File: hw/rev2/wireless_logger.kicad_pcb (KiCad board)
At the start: 4 copper layers, 147 parts, among them J1 FCI 10118194, J2 CONN_2, J3 SSD1306_SER, J4 SWD_10PIN, J5 CONN_5, P1 CONN_6X2, Q1 2N7002P, Q2 2N7002P, U1 MT29FXX01A, U10 CC2541, U11 STM32F40X_BGA176, U2 MAG3110, U3 MMA8452Q, U4 LPS331AP, U5 L3GD20, U6 MCP111T-315, U7 BQ24095, U8 TPS62698, U9 CC1101, X1 FA-128 26.0000MF10Z-W3, X2 9HT10-32.768KBZF-T, X3 FA-128 32.0000MF20X-K3, X4 XRCGB25M000F0L00R0, X5 9HT10-32.768KBZF-T

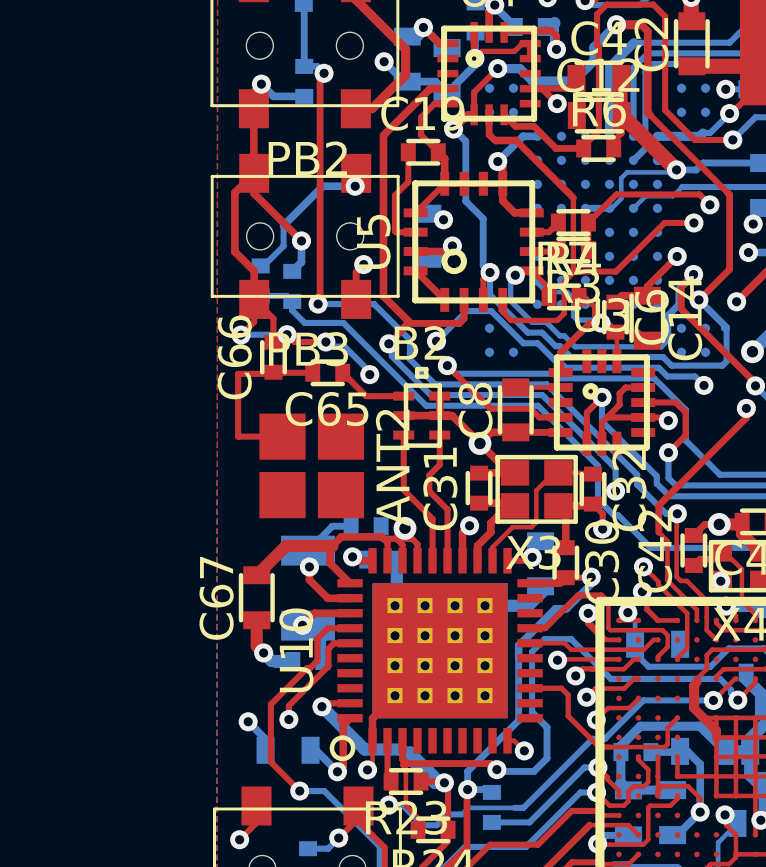
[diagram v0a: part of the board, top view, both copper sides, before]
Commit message: Minor rerouting stuffs
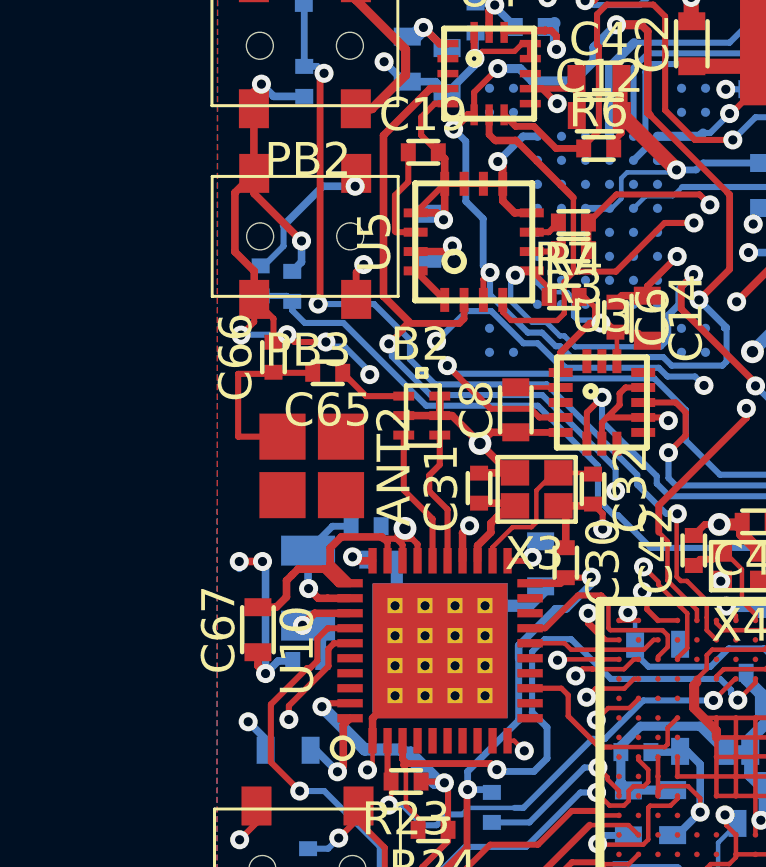
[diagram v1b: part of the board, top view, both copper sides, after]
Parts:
- moved C67 1.07 mm to (171.4, 138.8)
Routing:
- net GND: track 262.2 -> 268.0 mm, vias 54 -> 56
- net V3: track 321.9 -> 323.9 mm

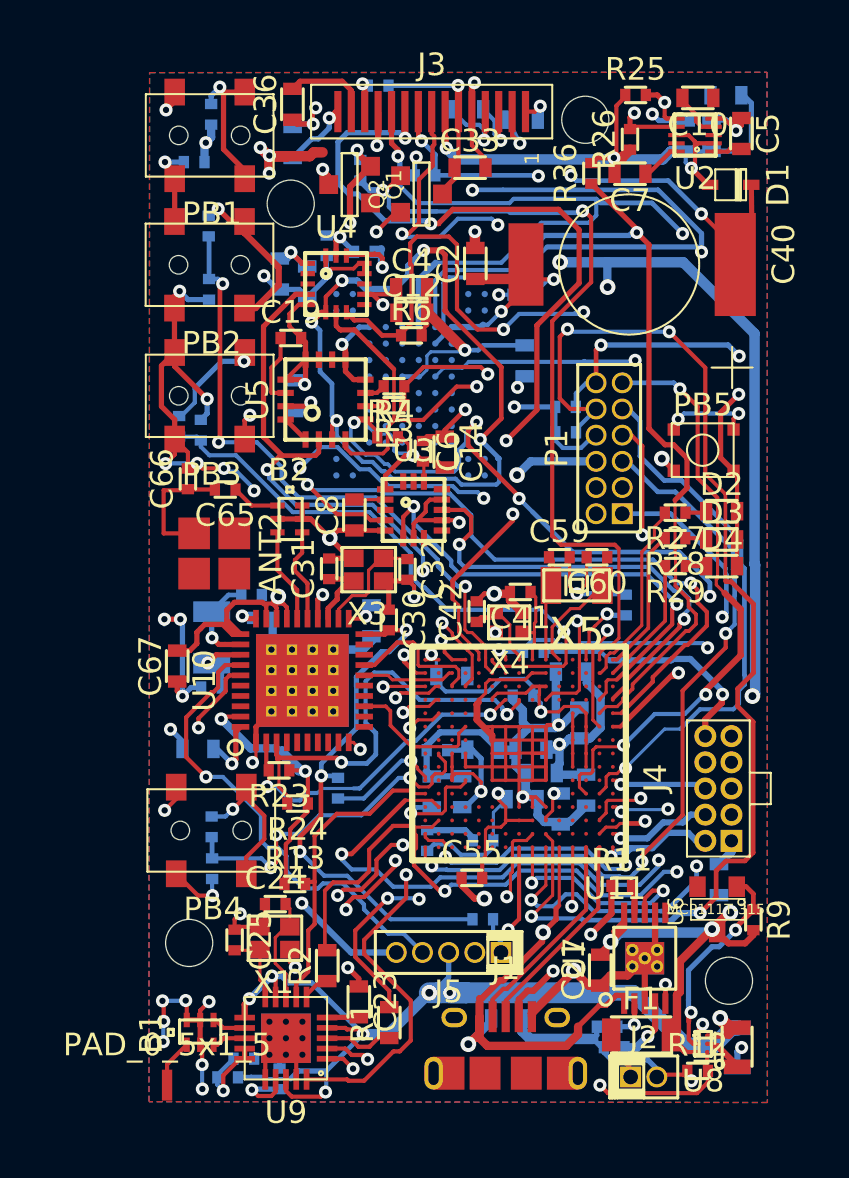
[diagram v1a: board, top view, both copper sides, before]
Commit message: STM32 checked -- Some optimization done on routes and important filtering bits
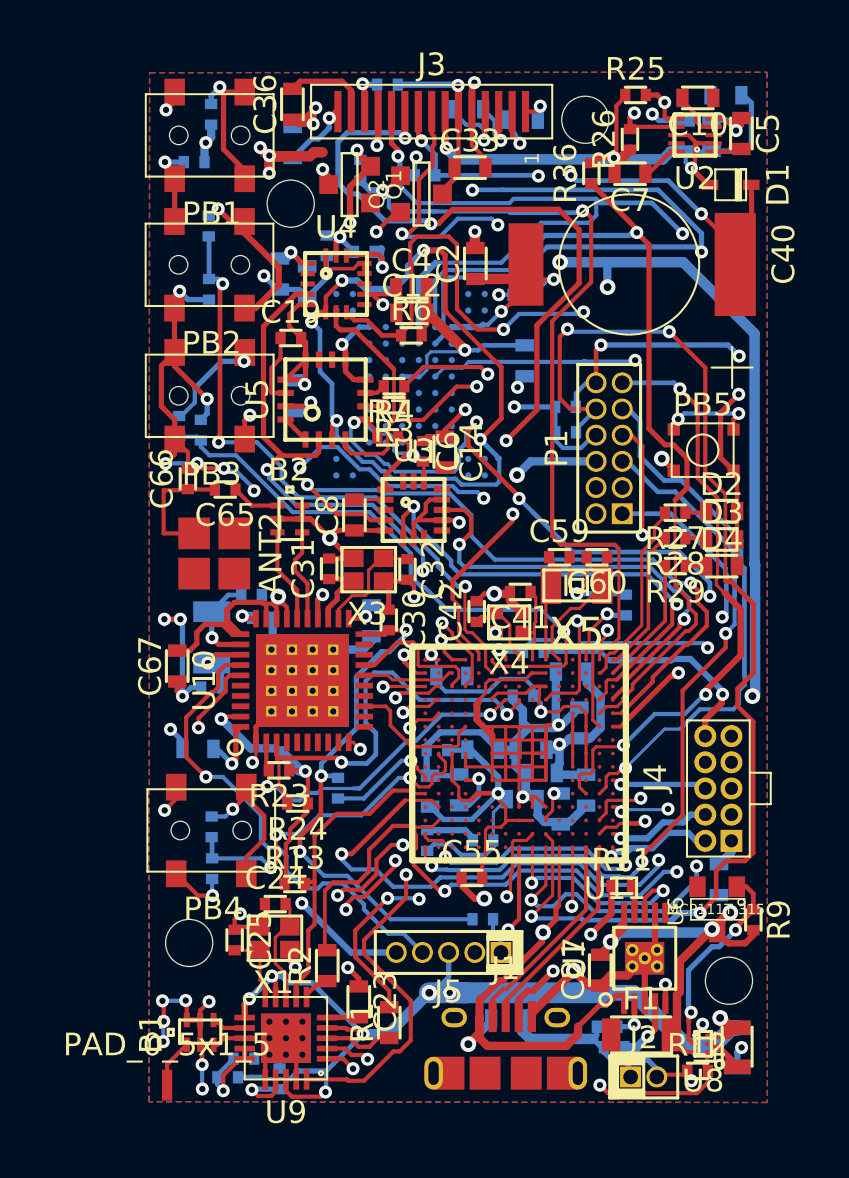
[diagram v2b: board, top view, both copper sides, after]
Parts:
- moved C45 1.55 mm to (183.6, 144.9)
- moved C44 1.33 mm to (185.1, 144.8)
- moved R21 0.45 mm to (181.6, 110.6)
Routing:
- net V3: track 323.9 -> 328.2 mm, vias 29 -> 28
- net N-0000063: track 5.17 -> 2.65 mm
- net /OLED/OLED_GND: track 17.4 -> 19.3 mm
- net GND: track 268.0 -> 269.3 mm

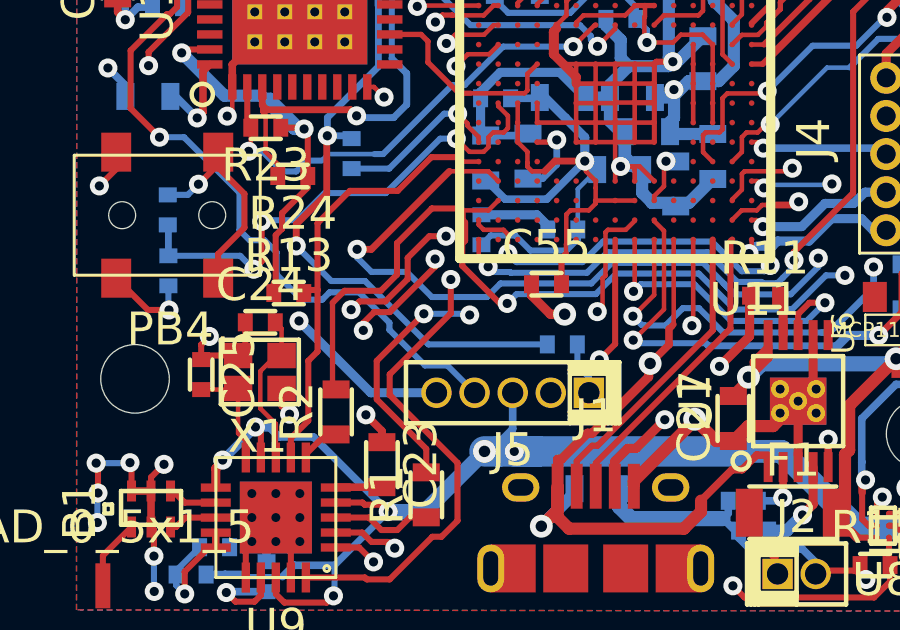
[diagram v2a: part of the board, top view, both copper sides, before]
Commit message: Fixed misconnected CC1101 debug output to SPI2
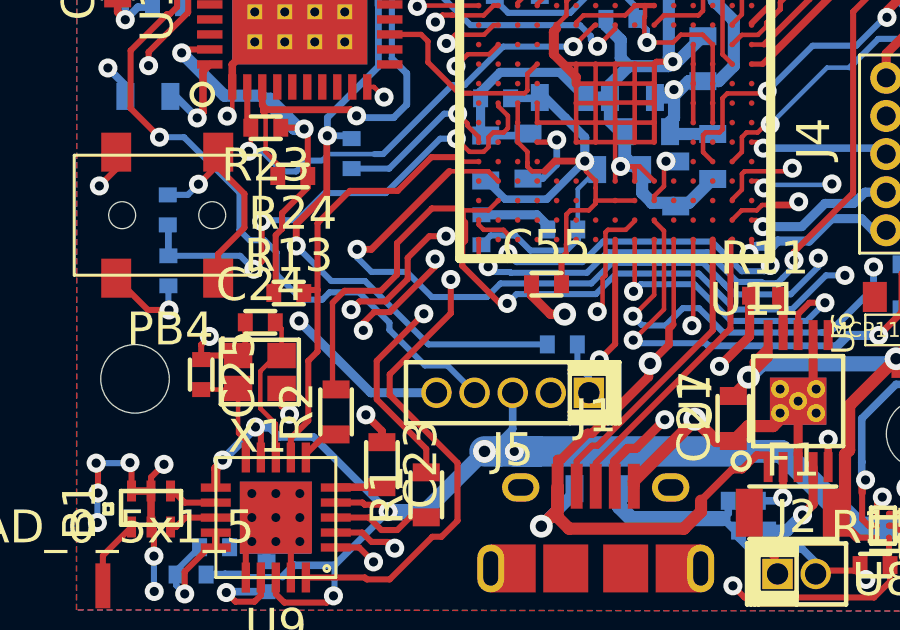
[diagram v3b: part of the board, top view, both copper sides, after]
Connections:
- R1 pad 2: /STM32F4/SPI2_MISO -> /STM32F4/SPI2_MOSI
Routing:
- net /STM32F4/SPI2_MISO: track 42.8 -> 32.1 mm, vias 4 -> 2
- net /STM32F4/SPI2_MOSI: track 36.6 -> 46.4 mm, vias 3 -> 4

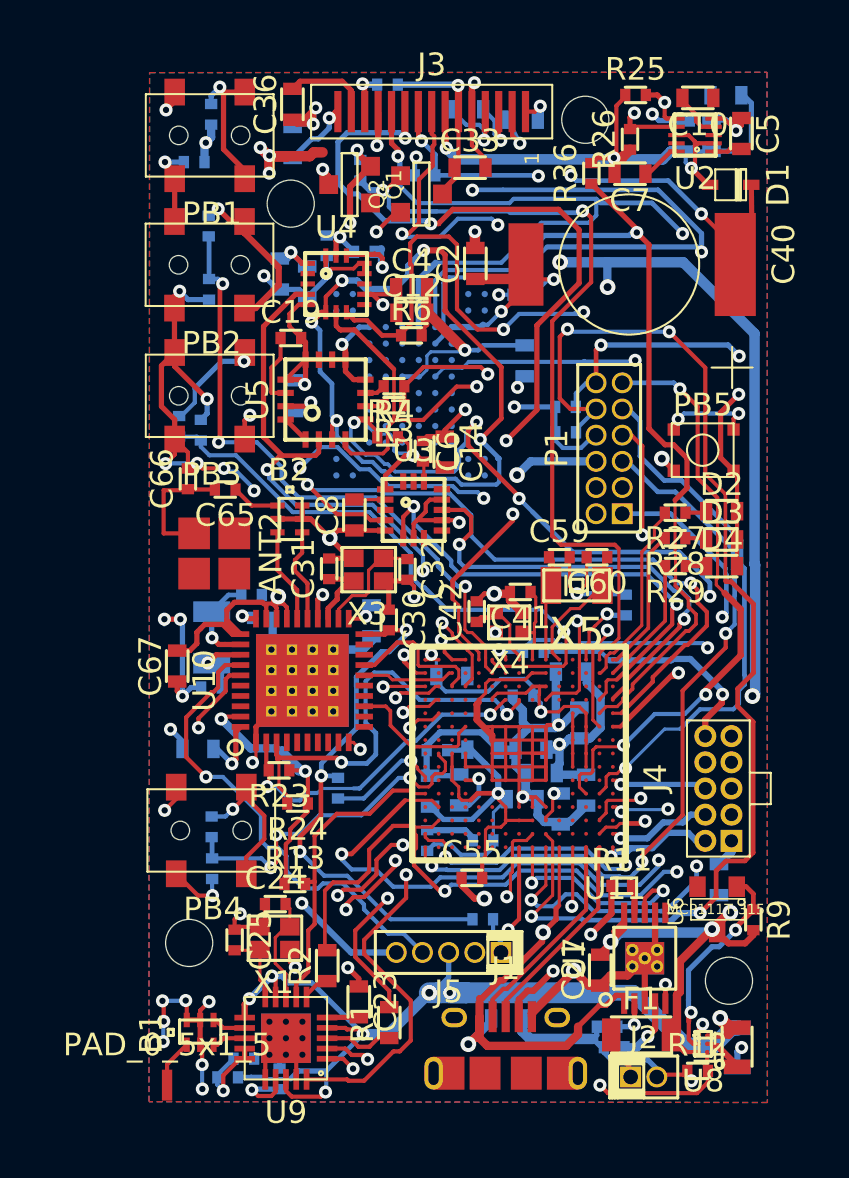
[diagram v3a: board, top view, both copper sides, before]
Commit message: Moved silks around!
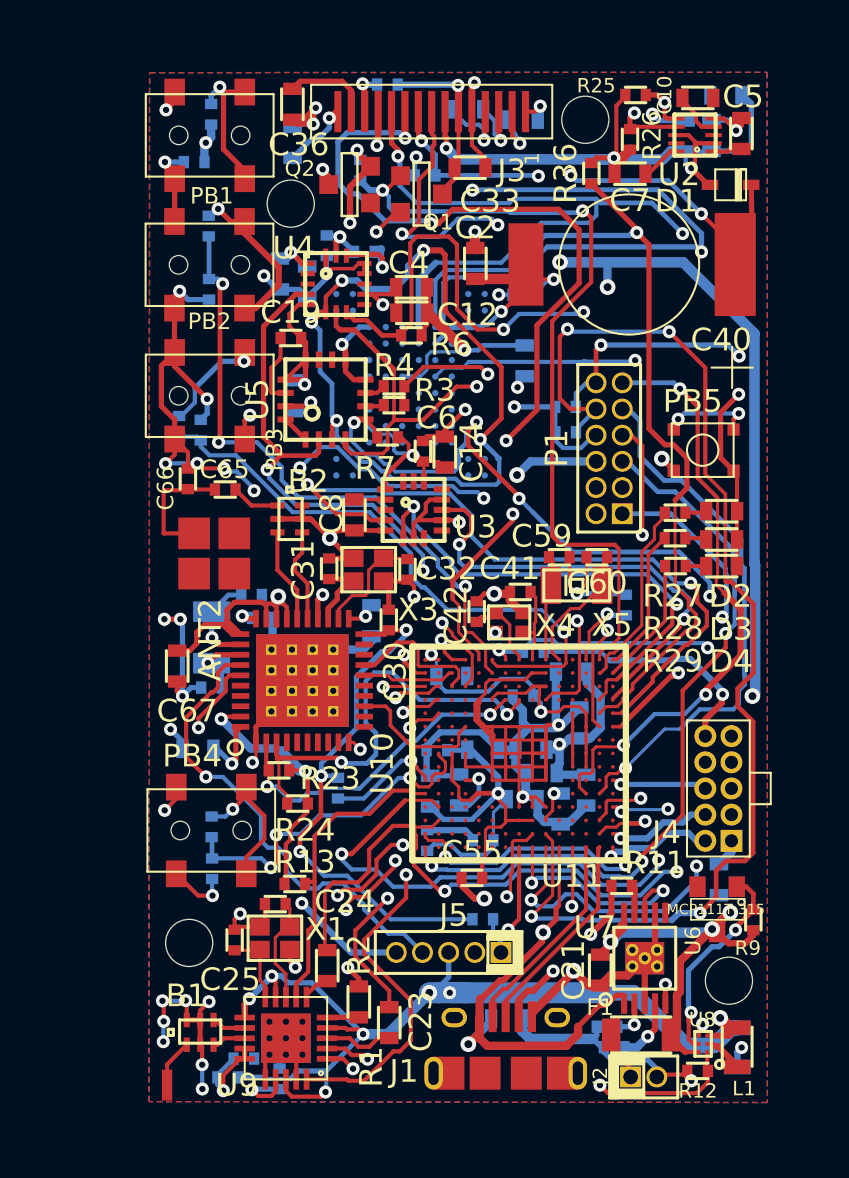
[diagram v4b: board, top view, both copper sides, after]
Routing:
- net (no net): track 5.00 -> 0.01 mm, vias 3 -> 0
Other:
- board text added: "+"
- board text added: "-"
- board text added: "2013 McGill IML"
- board text added: "rev 2a"

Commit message: Rev 2a submitted to OSH Park for manufacture
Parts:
- moved C50 0.92 mm to (188.0, 146.2)
- moved C6 0.16 mm to (183.3, 128.3)
- renumbered P1 to J6
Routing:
- net GND: track 269.3 -> 282.2 mm
- net N-00000167: track 28.6 -> 34.2 mm
- net /Sensors/GYR_SPI_MOSI: track 80.8 -> 85.1 mm, vias 7 -> 6
- net V3: track 328.2 -> 332.4 mm
- net /STM32F4/SPI2_NSS: track 51.5 -> 53.5 mm
- net /STM32F4/EXTI8: track 16.8 -> 18.6 mm
- net N-00000189: track 10.3 -> 12.1 mm
- net /STM32F4/OLED_nD/C: track 47.0 -> 48.6 mm
- net /Sensors/ACC_INT1: track 22.3 -> 23.8 mm
- net /Sensors/ACC_I2C_SCL: track 66.3 -> 67.7 mm
- net /Sensors/GYR_SPI_MISO: track 63.3 -> 62.1 mm
- net /Bluetooth/RF_RESET_N_LOCAL: track 25.8 -> 26.9 mm
- net /OLED/OLED_GND: track 19.3 -> 20.2 mm
- net /OLED/EN: track 39.9 -> 40.8 mm
- net /OLED/SDIN: track 68.1 -> 68.9 mm
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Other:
- board outline added: 30 x 50 mm
- net class 50OHM: via_dia 0.635 -> 0.6858; via_drill 0.3048 -> 0.3302
- net class Default: via_dia 0.635 -> 0.6858; via_drill 0.3048 -> 0.3302
- rule via_min_drill: 0.3048 -> 0.3302
- rule via_min_size: 0.635 -> 0.6858
- board text added: "1"
- board text added: "GND"
- board text added: "RST"
- board text added: "Strike Force rev 2a"
- board text added: "V3"
- board text added: "Vbat"
- board text added: "Vbus"
- board text removed: "rev 2a"

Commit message: Set soldermask clearance to zero
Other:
- rule pad_to_mask_clearance: 0.2 -> 0
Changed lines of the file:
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@@
   )
   (setup
-    (last_trace_width 0.254)
+    (last_trace_width 0.1524)
     (user_trace_width 0.1524)
     (user_trace_width 0.1778)
@@
     (pad_size 0.6 0.6)
     (pad_drill 0.3302)
-    (pad_to_mask_clearance 0.2)
+    (pad_to_mask_clearance 0)
     (aux_axis_origin 0 0)
     (visible_elements FFFF7FBF)

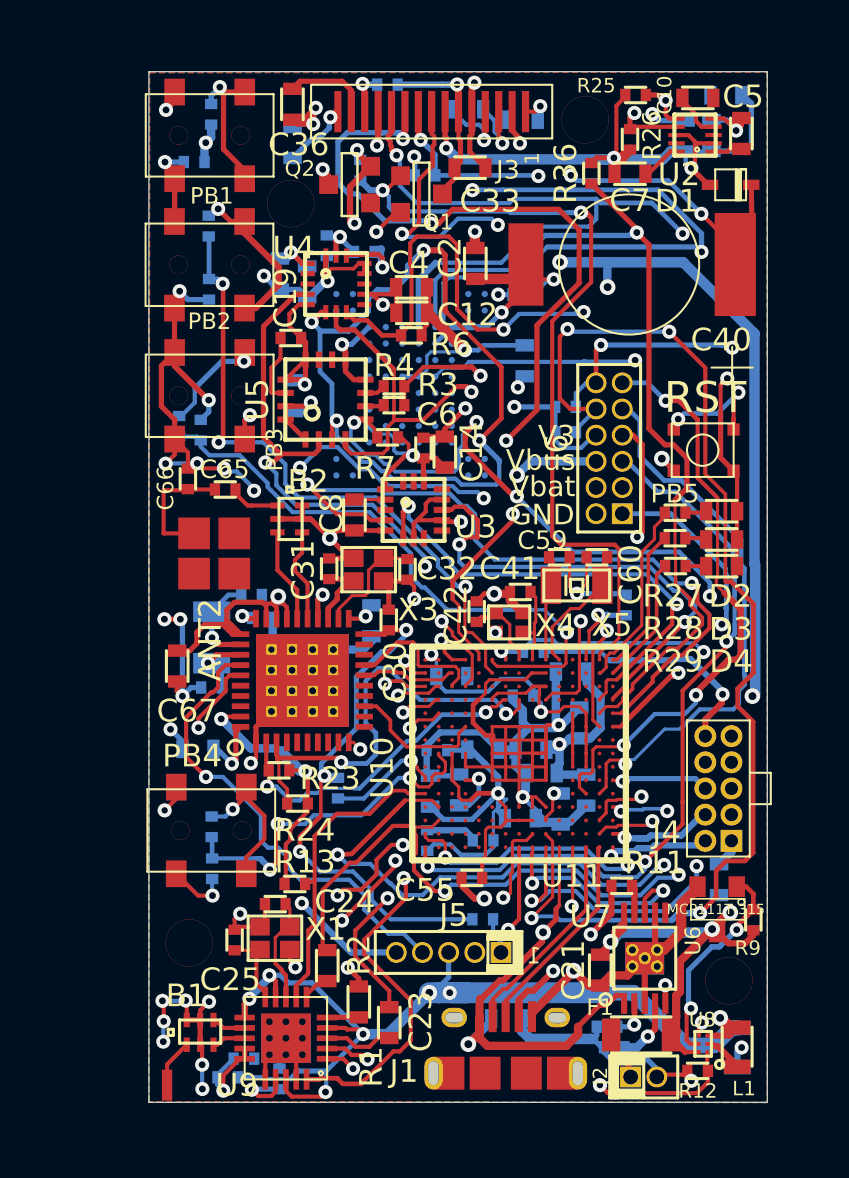
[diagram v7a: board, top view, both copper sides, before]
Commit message: Updated PCB to 5 mil trace/space for more-reasonably-sized BGA pads
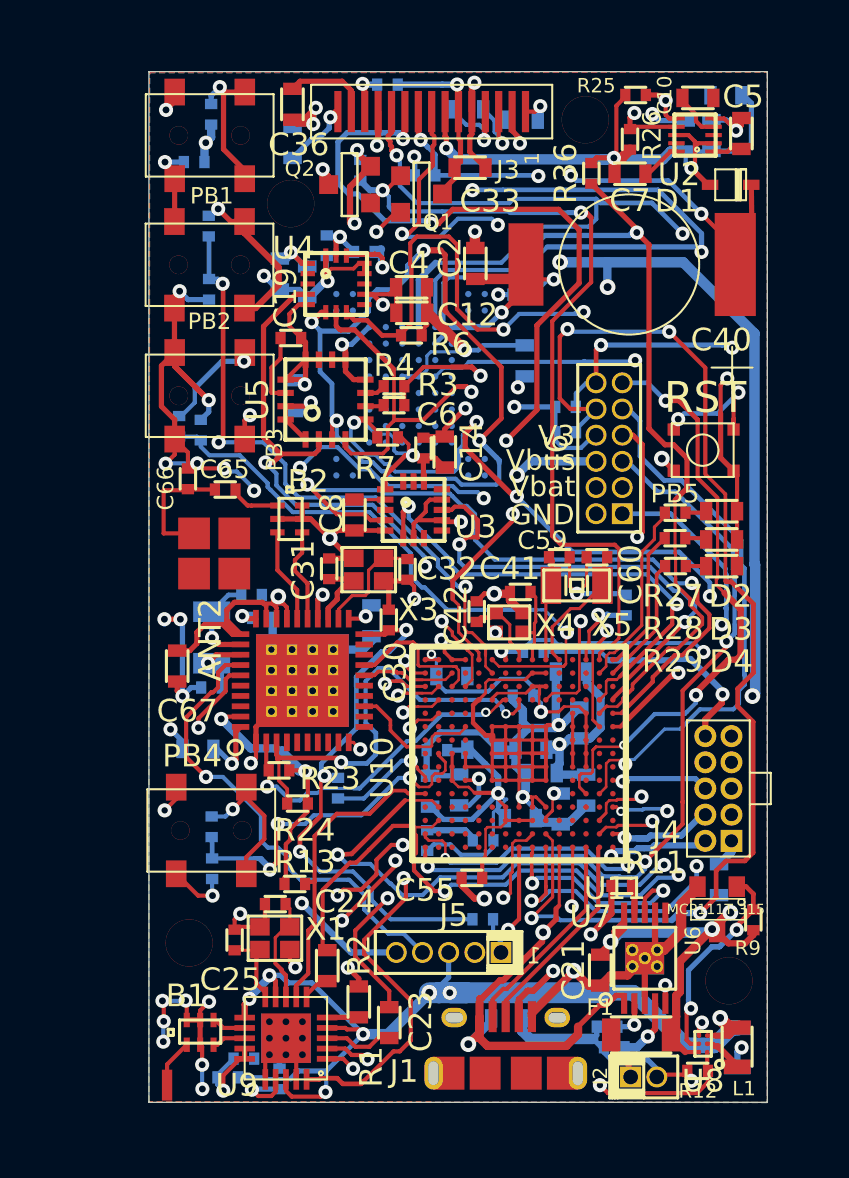
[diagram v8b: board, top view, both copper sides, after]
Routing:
- net /Sensors/GYR_SPI_CLK: track 56.6 -> 57.4 mm
- net /STM32F4/UART2_TX: track 28.9 -> 29.4 mm
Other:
- net class Default: clearance 0.1524 -> 0.127
- rule trace_clearance: 0.1524 -> 0.127
- rule trace_min: 0.1524 -> 0.127
- rule via_min_drill: 0.3302 -> 0.254
- rule via_min_size: 0.6858 -> 0.4572
